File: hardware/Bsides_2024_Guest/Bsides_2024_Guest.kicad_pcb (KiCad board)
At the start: 2 copper layers, 134.5 x 129.5 mm, 45 parts, among them J1 Add_On, J2 Battery, J3 Battery, J4 OLED, J5 Serial_IN, J6 Serial_OUT, P1 USB_C_Plug_USB2.0, Q1 DMG3415U-7, SW1 ON, SW2 RESET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

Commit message: Update route and schematic
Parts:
- moved J6 2.04 mm to (69.9, 141.0)
- moved J4 0.17 mm to (69.3, 124.0)
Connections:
- net /GPIO15 renamed /RIGHT
- C11 pad 2: /GPIO23 -> /DOWN
- C8 pad 2: /GPIO1 -> /LEFT
- C9 pad 2: /GPIO22 -> /UP
- SW4 pad 2: /GPIO1 -> /UP
- SW5 pad 2: /GPIO22 -> /DOWN
- SW7 pad 2: /GPIO23 -> /LEFT
- U1 pad 20: /GPIO22 -> /UP
- U1 pad 21: /GPIO23 -> /DOWN
- U1 pad 9: /GPIO1 -> /LEFT
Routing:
- net /SCL: track 71.1 -> 110.2 mm, vias 0 -> 1
- net /SDA: track 73.8 -> 112.3 mm, vias 0 -> 1
- net /LEFT: track 0.00 -> 11.0 mm
- net /GPIO1: track 11.0 -> 0.00 mm
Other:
- outline, holes or cut-outs redrawn
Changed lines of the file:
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@@
 	(net 4 "/BOOT")
 	(net 5 "/EN")
-	(net 6 "/GPIO1")
-	(net 7 "/GPIO22")
-	(net 8 "/GPIO15")
-	(net 9 "/GPIO23")
+	(net 6 "/LEFT")
+	(net 7 "/UP")
+	(net 8 "/RIGHT")
+	(net 9 "/DOWN")
 	(net 10 "Net-(D1-K)")
 	(net 11 "VBUS")
@@
 	(footprint "bsides:Display OLED 128 x32"
 		(layer "F.Cu")
-		(at 69.11 123.98)
+		(at 69.28 123.98)
 		(descr "Through hole straight pin header, 1x04, 2.54mm pitch, single row")
 		(tags "Through hole pin header THT 1x04 2.54mm single row")
@@
 		(tags "LED RGB NeoPixel Mini")
 		(property "Reference" "D3"
-			(at 0 -2.75 360)
+			(at 0 -2.75 0)
 			(layer "F.SilkS")
 			(effects
@@
 		)
 		(property "Value" "WS2812B"
-			(at 0 3.25 360)
+			(at 0 3.25 0)
 			(layer "F.Fab")
 			(effects
@@
 		)
 		(fp_text user "1"
-			(at -3.1 -0.85 360)
+			(at -3.1 -0.85 0)
 			(layer "F.SilkS")
 			(effects
@@
 		)
 		(fp_text user "${REFERENCE}"
-			(at 0 0 360)
+			(at 0 0 0)
 			(layer "F.Fab")
 			(effects
@@
 	(footprint "Connector_PinSocket_2.54mm:PinSocket_1x03_P2.54mm_Vertical"
 		(layer "F.Cu")
-		(at 68.479527 139.532568 -134.889)
+		(at 69.87 141.02 -134.889)
 		(descr "Through hole straight socket strip, 1x03, 2.54mm pitch, single row (from Kicad 4.0.7), script generated")
 		(tags "Through hole socket strip THT 1x03 2.54mm single row")
@@
 			(size 1.5 0.9)
 			(layers "B.Cu" "B.Paste" "B.Mask")
-			(net 6 "/GPIO1")
+			(net 6 "/LEFT")
 			(pinfunction "IO1")
 			(pintype "bidirectional")
@@
 			(size 1.5 0.9)
 			(layers "B.Cu" "B.Paste" "B.Mask")
-			(net 7 "/GPIO22")
+			(net 7 "/UP")
 			(pinfunction "IO22")
 			(pintype "bidirectional")
@@
 			(size 1.5 0.9)
 			(layers "B.Cu" "B.Paste" "B.Mask")
-			(net 9 "/GPIO23")
+			(net 9 "/DOWN")
 			(pinfunction "IO23")
 			(pintype "bidirectional")
@@
 			(size 1.5 0.9)
 			(layers "B.Cu" "B.Paste" "B.Mask")
-			(net 8 "/GPIO15")
+			(net 8 "/RIGHT")
 			(pinfunction "IO15")
 			(pintype "power_in")
@@
 		(tags "SOT TO_SOT_SMD")
 		(property "Reference" "U2"
-			(at 0 2.4 360)
+			(at 0 2.4 0)
 			(layer "B.SilkS")
 			(effects
@@
 		)
 		(property "Value" "AP2112K-3.3"
-			(at 0 -2.4 360)
+			(at 0 -2.4 0)
 			(layer "B.Fab")
 			(effects
@@
 		)
 		(fp_text user "${REFERENCE}"
-			(at 0 0 360)
+			(at 0 0 0)
 			(layer "B.Fab")
 			(effects
@@
 			(layers "B.Cu" "B.Paste" "B.Mask")
 			(roundrect_rratio 0.25)
-			(net 7 "/GPIO22")
+			(net 7 "/UP")
 			(pintype "passive")
 		)
@@
 			(at 0 -3.75 180)
 			(layer "B.Fab")
+			(hide yes)
 			(effects
 				(font
@@
 			(size 1.7 1)
 			(layers "B.Cu" "B.Paste" "B.Mask")
-			(net 8 "/GPIO15")
+			(net 8 "/RIGHT")
 			(pinfunction "2")
 			(pintype "passive")
@@
 			(size 1.7 1)
 			(layers "B.Cu" "B.Paste" "B.Mask")
-			(net 8 "/GPIO15")
+			(net 8 "/RIGHT")
 			(pinfunction "2")
 			(pintype "passive")
@@
 			(at 0 -3.75 180)
 			(layer "B.Fab")
+			(hide yes)
 			(effects
 				(font
@@
 			(size 1.7 1)
 			(layers "B.Cu" "B.Paste" "B.Mask")
-			(net 7 "/GPIO22")
+			(net 9 "/DOWN")
 			(pinfunction "2")
 			(pintype "passive")
@@
 			(size 1.7 1)
 			(layers "B.Cu" "B.Paste" "B.Mask")
-			(net 7 "/GPIO22")
+			(net 9 "/DOWN")
 			(pinfunction "2")
 			(pintype "passive")
@@
 			(at 0 -3.75 180)
 			(layer "B.Fab")
+			(hide yes)
 			(effects
 				(font
@@
 			(size 1.7 1)
 			(layers "B.Cu" "B.Paste" "B.Mask")
-			(net 9 "/GPIO23")
+			(net 6 "/LEFT")
 			(pinfunction "2")
 			(pintype "passive")
@@
 			(size 1.7 1)
 			(layers "B.Cu" "B.Paste" "B.Mask")
-			(net 9 "/GPIO23")
+			(net 6 "/LEFT")
 			(pinfunction "2")
 			(pintype "passive")
@@
 			(at 0 -3.75 180)
 			(layer "B.Fab")
+			(hide yes)
 			(effects
 				(font
@@
 			(size 1.7 1)
 			(layers "B.Cu" "B.Paste" "B.Mask")
-			(net 6 "/GPIO1")
+			(net 7 "/UP")
 			(pinfunction "2")
 			(pintype "passive")
@@
 			(size 1.7 1)
 			(layers "B.Cu" "B.Paste" "B.Mask")
-			(net 6 "/GPIO1")
+			(net 7 "/UP")
 			(pinfunction "2")
 			(pintype "passive")
@@
 		(fp_arc
 			(start -2.4 3.300001)
-			(mid -2.450001 3.349991)
+			(mid -2.45 3.349989)
 			(end -2.500001 3.299999)
 			(stroke
@@
 			(layers "B.Cu" "B.Paste" "B.Mask")
 			(roundrect_rratio 0.25)
-			(net 8 "/GPIO15")
+			(net 8 "/RIGHT")
 			(pintype "passive")
 		)
@@
 		(tags "SOT TO_SOT_SMD")
 		(property "Reference" "Q1"
-			(at 0 2.4 360)
+			(at 0 2.4 0)
 			(layer "B.SilkS")
 			(effects
@@
 		)
 		(property "Value" "DMG3415U-7"
-			(at 0 -2.4 360)
+			(at 0 -2.4 0)
 			(layer "B.Fab")
 			(effects
@@
 		)
 		(fp_text user "${REFERENCE}"
-			(at 0 0 360)
+			(at 0 0 0)
 			(layer "B.Fab")
 			(effects
@@
 		(tags "resistor")
 		(property "Reference" "R2"
-			(at 0 1.43 360)
+			(at 0 1.43 0)
 			(layer "B.SilkS")
 			(effects
@@
 		)
 		(property "Value" "100K"
-			(at 0 -1.43 360)
+			(at 0 -1.43 0)
 			(layer "B.Fab")
 			(effects
@@
 		)
 		(fp_text user "${REFERENCE}"
-			(at 0 0 360)
+			(at 0 0 0)
 			(layer "B.Fab")
 			(effects
@@
 		(tags "resistor")
 		(property "Reference" "R6"
-			(at 0 1.43 360)
+			(at 0 1.43 0)
 			(layer "B.SilkS")
 			(effects
@@
 		)
 		(property "Value" "470"
-			(at 0 -1.43 360)
+			(at 0 -1.43 0)
 			(layer "B.Fab")
 			(effects
@@
 		)
 		(fp_text user "${REFERENCE}"
-			(at 0 0 360)
+			(at 0 0 0)
 			(layer "B.Fab")
 			(effects
@@
 		(tags "capacitor")
 		(property "Reference" "C5"
-			(at 0 1.43 360)
+			(at 0 1.43 0)
 			(layer "B.SilkS")
 			(effects
@@
 		)
 		(property "Value" "0.1uF"
-			(at 0 -1.43 360)
+			(at 0 -1.43 0)
 			(layer "B.Fab")
 			(effects
@@
 		)
 		(fp_text user "${REFERENCE}"
-			(at 0 0 360)
+			(at 0 0 0)
 			(layer "B.Fab")
 			(effects
@@
 			(layers "B.Cu" "B.Paste" "B.Mask")
 			(roundrect_rratio 0.25)
-			(net 9 "/GPIO23")
+			(net 9 "/DOWN")
 			(pintype "passive")
 		)
@@
 			(layers "B.Cu" "B.Paste" "B.Mask")
 			(roundrect_rratio 0.25)
-			(net 6 "/GPIO1")
+			(net 6 "/LEFT")
 			(pintype "passive")
 		)
@@
 		(layer "Edge.Cuts")
 	)
+	(gr_line
+		(start 58.25 131.97)
+		(end 63.633202 137.332572)
+		(stroke
+			(width 0.05)
+			(type default)
+		)
+		(layer "Edge.Cuts")
+	)
 	(gr_curve
 		(pts
@@
 	)
 	(segment
+		(start 67.864683 122.925124)
+		(end 67.864683 125.944683)
+		(width 0.3)
+		(layer "F.Cu")
+		(net 22)
+	)
+	(segment
+		(start 91.53 119.32)
+		(end 89.56 121.29)
+		(width 0.3)
+		(layer "F.Cu")
+		(net 22)
+	)
+	(segment
+		(start 68.44 126.52)
+		(end 69.28 126.52)
+		(width 0.3)
+		(layer "F.Cu")
+		(net 22)
+	)
+	(segment
+		(start 89.56 121.29)
+		(end 69.439665 121.29)
+		(width 0.3)
+		(layer "F.Cu")
+		(net 22)
+	)
+	(segment
+		(start 91.539927 110.109927)
+		(end 91.53 110.119854)
+		(width 0.3)
+		(layer "F.Cu")
+		(net 22)
+	)
+	(segment
+		(start 69.439665 121.29)
+		(end 67.864683 122.925124)
+		(width 0.3)
+		(layer "F.Cu")
+		(net 22)
+	)
+	(segment
+		(start 91.53 110.119854)
+		(end 91.53 119.32)
+		(width 0.3)
+		(layer "F.Cu")
+		(net 22)
+	)
+	(segment
+		(start 67.864683 125.944683)
+		(end 68.44 126.52)
+		(width 0.3)
+		(layer "F.Cu")
+		(net 22)
+	)
+	(via
+		(at 91.539927 110.109927)
+		(size 0.6)
+		(drill 0.3)
+		(layers "F.Cu" "B.Cu")
+		(net 22)
+	)
+	(segment
 		(start 90.252883 111.396971)
 		(end 125.059854 76.59)
@@
 	)
 	(segment
-		(start 123.974072 75.88)
-		(end 143.205526 75.88)
+		(start 92.197036 107.657036)
+		(end 92.19 107.664072)
 		(width 0.3)
-		(layer "B.Cu")
+		(layer "F.Cu")
 		(net 23)
 	)
 	(segment
-		(start 89.339319 110.514753)
+		(start 92.19 107.664072)
+		(end 92.19 122.73)
+		(width 0.3)
+		(layer "F.Cu")
+		(net 23)
+	)
+	(segment
+		(start 90.94 123.98)
+		(end 69.28 123.98)
+		(width 0.3)
+		(layer "F.Cu")
+		(net 23)
+	)
+	(segment
+		(start 92.19 122.73)
+		(end 90.94 123.98)
+		(width 0.3)
+		(layer "F.Cu")
+		(net 23)
+	)
+	(via
+		(at 92.197036 107.657036)
+		(size 0.6)
+		(drill 0.3)
+		(layers "F.Cu" "B.Cu")
+		(net 23)
+	)
+	(segment
+		(start 92.197036 107.657036)
 		(end 123.974072 75.88)
 		(width 0.3)
@@
 	)
 	(segment
-		(start 143.205526 75.88)
-		(end 145.091143 73.994383)
+		(start 123.974072 75.88)
+		(end 143.205526 75.88)
 		(width 0.3)
 		(layer "B.Cu")
@@
 	)
 	(segment
-		(start 145.091143 73.988857)
-		(end 146.66284 72.41716)
+		(start 143.205526 75.88)
+		(end 145.091143 73.994383)
 		(width 0.3)
 		(layer "B.Cu")
@@
 	)
 	(segment
-		(start 145.091143 73.994383)
-		(end 145.091143 73.988857)
+		(start 89.339319 110.514753)
+		(end 92.197036 107.657036)
 		(width 0.3)
 		(layer "B.Cu")
@@
 		(width 0.3)
 		(layer "B.Cu")
+		(net 23)
+	)
+	(segment
+		(start 145.091143 73.988857)
+		(end 146.66284 72.41716)
+		(width 0.3)
+		(layer "B.Cu")
+		(net 23)
+	)
+	(segment
+		(start 145.091143 73.994383)
+		(end 145.091143 73.988857)
+		(width 0.3)
+		(layer "B.Cu")

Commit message: Feat(Hw): Update PCB
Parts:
- J6: moved to B.Cu
- moved J5 1.79 mm to (181.5, 145.8)
- moved J6 0.19 mm to (69.7, 140.9), turned to 45.111 degrees
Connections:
- C10 pad 2: /RIGHT -> /LEFT
- C11 pad 2: /DOWN -> /RIGHT
- C8 pad 2: /LEFT -> /UP
- C9 pad 2: /UP -> /DOWN
- SW6 pad 2: /RIGHT -> /LEFT
- SW7 pad 2: /LEFT -> /RIGHT
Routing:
- net /VOUT: track 6.05 -> 426.1 mm, vias 0 -> 14
- net Net-(D3-DOUT): track 2.54 -> 155.5 mm, vias 1 -> 4
- net /BOOT: track 0.00 -> 127.9 mm, vias 0 -> 6
- net /GPIO16: track 0.00 -> 127.6 mm, vias 0 -> 3
- net /GPIO17: track 0.00 -> 125.2 mm, vias 0 -> 3
- net /GPIO3: track 0.00 -> 115.2 mm, vias 0 -> 4
- net /GPIO2: track 0.00 -> 111.0 mm, vias 0 -> 4
- net Net-(D4-DOUT): track 0.00 -> 98.1 mm, vias 0 -> 2
- net /PIN: track 32.4 -> 105.8 mm, vias 0 -> 2
- net /DOWN: track 0.00 -> 64.4 mm
- net /UP: track 0.00 -> 50.8 mm, vias 0 -> 2
- net /GPIO4: track 0.00 -> 47.8 mm, vias 0 -> 1
- net /GPIO5: track 0.00 -> 47.7 mm, vias 0 -> 2
- net /EN: track 0.00 -> 42.7 mm
- net /LEFT: track 11.0 -> 43.9 mm, vias 0 -> 2
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- added copper zone on B.Cu, net GND
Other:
- outline, holes or cut-outs redrawn

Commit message: feat(Hw): Update route
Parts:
- moved R3 0.12 mm to (173.4, 133.2)
- moved F1 0.11 mm to (172.1, 132.1)
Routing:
- net GND: track 17.7 -> 63.2 mm, vias 14 -> 32
- net /D-: track 100.5 -> 103.6 mm
- net /D+: track 100.5 -> 103.4 mm
- removed copper zone on F.Cu, net (none)

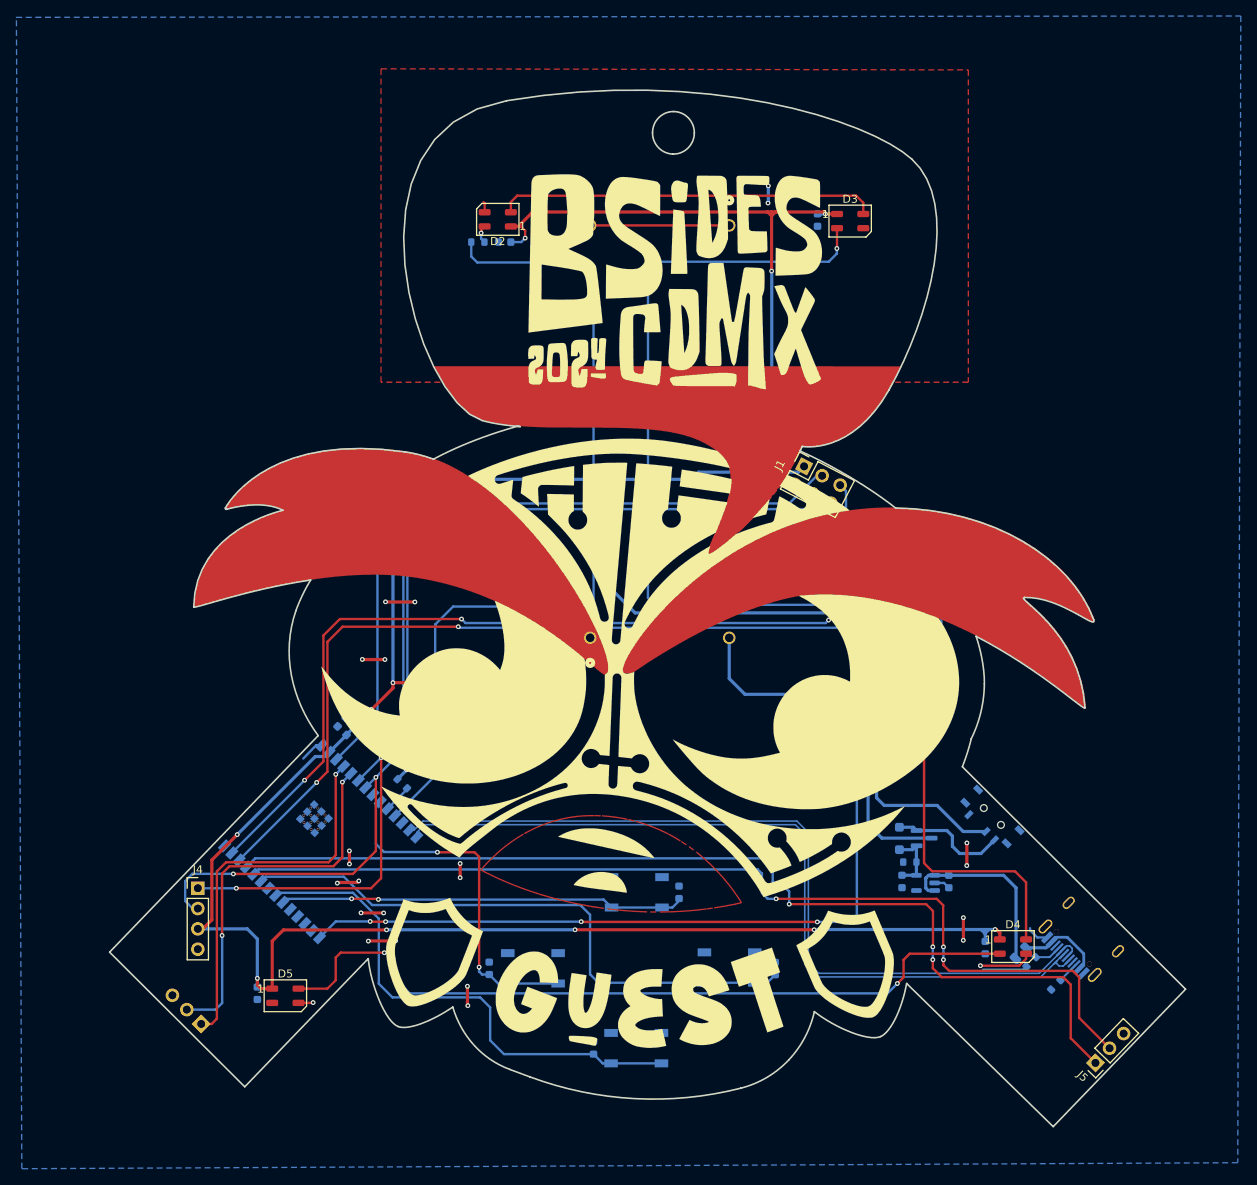
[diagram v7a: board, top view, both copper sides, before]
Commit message: feat(Hw):Update_BOM_Added_Labels
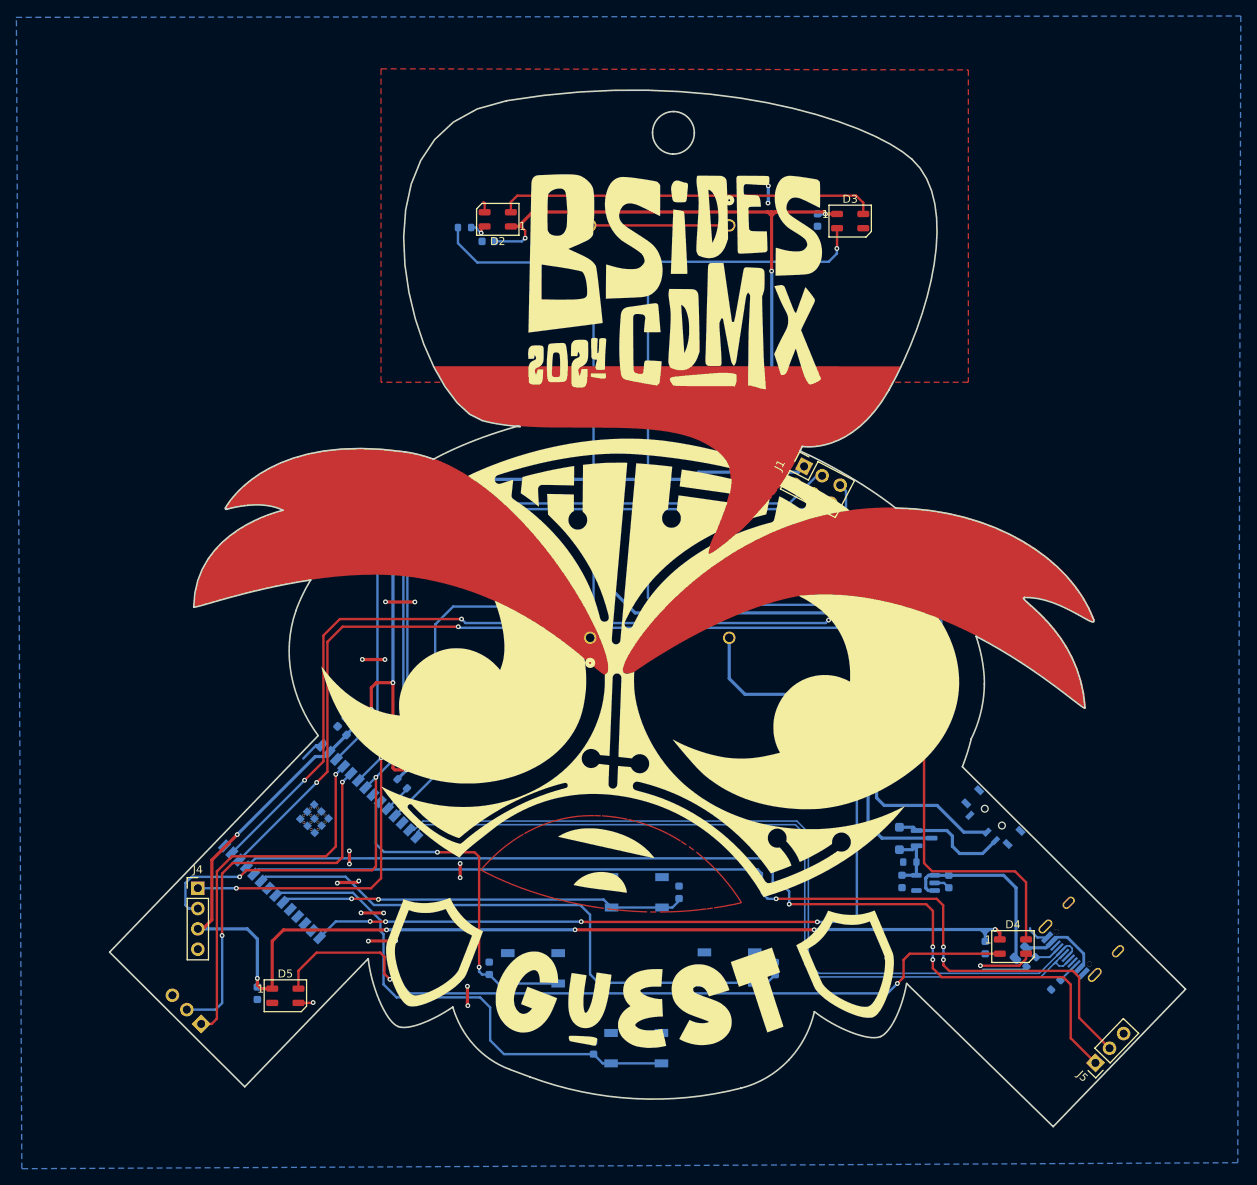
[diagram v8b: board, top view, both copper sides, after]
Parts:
- added kibuzzard-666B5E08: G***, kibuzzard-666B5E08, B.Cu at (169.4, 120.1)
- added kibuzzard-666B5E3B: G***, kibuzzard-666B5E3B, B.Cu at (163.6, 114.7)
- added kibuzzard-666B5E64: G***, kibuzzard-666B5E64, B.Cu at (135.5, 137.6)
- added kibuzzard-666B5E88: G***, kibuzzard-666B5E88, B.Cu at (124.3, 147.6)
- added kibuzzard-666B5E96: G***, kibuzzard-666B5E96, B.Cu at (110.9, 137.9)
- added kibuzzard-666B5EA2: G***, kibuzzard-666B5EA2, B.Cu at (124.2, 128.2)
- added kibuzzard-666B5EBB: G***, kibuzzard-666B5EBB, B.Cu at (88.3, 71.7)
- added kibuzzard-666B5ECE: G***, kibuzzard-666B5ECE, B.Cu at (167.8, 81.9)
- moved R6 2.46 mm to (102.6, 41.4)
- moved C5 2.05 mm to (105.6, 43.1)
- moved SW1 0.14 mm to (168.7, 115.1)
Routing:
- net GND: track 63.2 -> 53.5 mm, vias 32 -> 30
- net /VOUT: track 426.1 -> 428.7 mm
- net /PIN: track 105.8 -> 108.3 mm
- net /SCL: track 127.2 -> 128.4 mm
- net /GPIO4: track 47.8 -> 47.2 mm
